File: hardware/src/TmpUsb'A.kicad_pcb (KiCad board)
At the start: 2 copper layers, 25 x 17 mm, 17 parts, among them P1 48037-2200, U1 PIC18F26J50

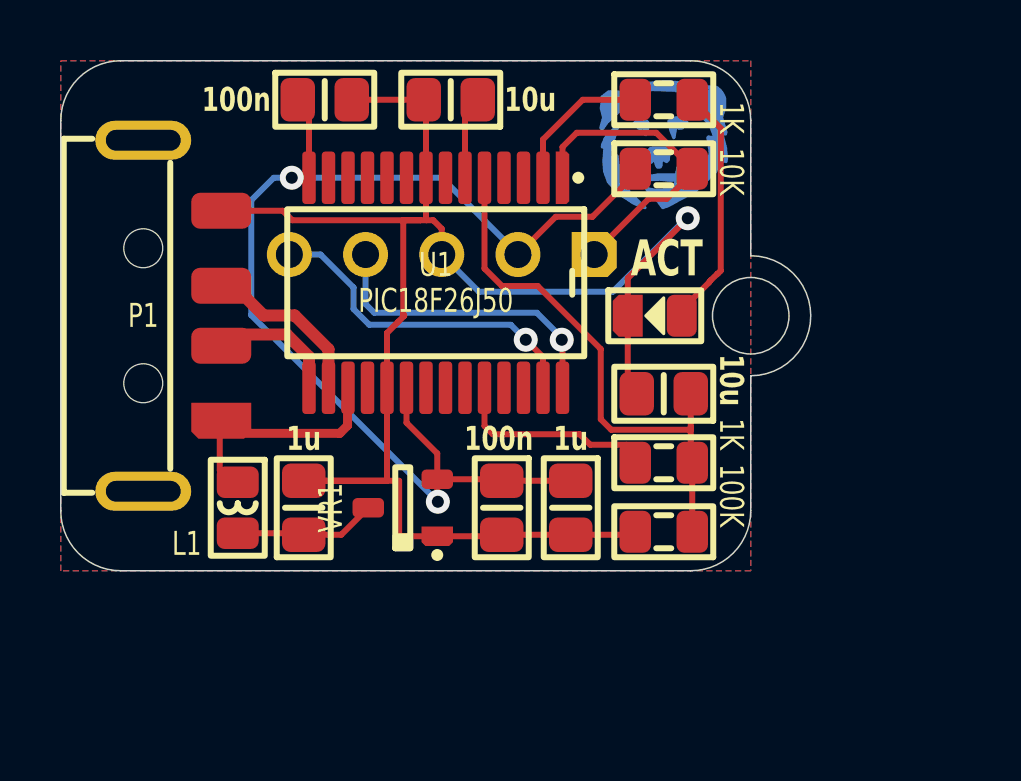
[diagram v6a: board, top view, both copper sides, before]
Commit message: Fixing connector designators
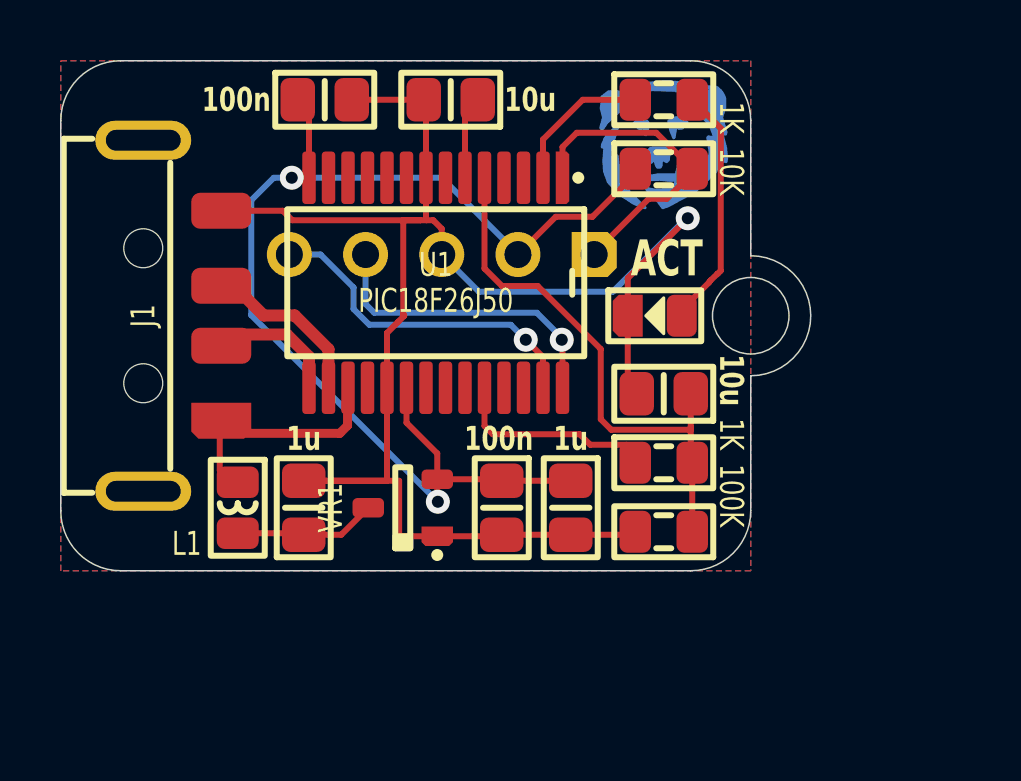
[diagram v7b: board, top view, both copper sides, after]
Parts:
- J1: renamed from P1; footprint Medo64:P USB A 2.0 (4w) -> Medo64:J USB A 2.0 Plug (4w)
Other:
- rule pad_to_mask_clearance: 0 -> 0.05
- board text added: "TmpUsb'A BXXXX"
- board text removed: "TmpUsb'A B"
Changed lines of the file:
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@@
 			(dielectric_constraints no)
 		)
-		(pad_to_mask_clearance 0)
+		(pad_to_mask_clearance 0.05)
 		(allow_soldermask_bridges_in_footprints no)
 		(aux_axis_origin 15 15)
@@
 		)
 	)
-	(footprint "Medo64:P USB A 2.0 (4w)"
+	(footprint "Medo64:J USB A 2.0 Plug (4w)"
 		(layer "F.Cu")
 		(at 17.75 23.5 -90)
-		(property "Reference" "P1"
-			(at 0 0 0)
-			(unlocked yes)
+		(property "Reference" "J1"
+			(at 0 0 -90)
 			(layer "F.SilkS")
 			(effects
@@
 		(property "Value" "48037-2200"
 			(at 0 1.6 -90)
-			(unlocked yes)
 			(layer "F.SilkS")
 			(hide yes)
@@
 			)
 		)
-		(property "Footprint" "Medo64:P USB A 2.0 (4w)"
+		(property "Footprint" "Medo64:J USB A 2.0 Plug (4w)"
 			(at 0 0 -90)
 			(unlocked yes)
@@
 			(layer "F.Fab")
 		)
-		(fp_text user "D-"
-			(at 1 -1.5 -90)
-			(unlocked yes)
+		(fp_text user "Vbus"
+			(at 3.5 -1.4 -90)
 			(layer "Cmts.User" knockout)
 			(effects
@@
 					(size 0.13 0.07)
 					(thickness 0.01)
+					(bold yes)
 				)
-				(justify top)
 			)
 		)
 		(fp_text user "GND"
-			(at -3.5 -1.5 -90)
-			(unlocked yes)
+			(at -3.5 -1.4 -90)
 			(layer "Cmts.User" knockout)
 			(effects
@@
 					(bold yes)
 				)
-				(justify top)
 			)
 		)
-		(fp_text user "Vbus"
-			(at 3.5 -1.5 -90)
-			(unlocked yes)
+		(fp_text user "D-"
+			(at 1 -1.4 -90)
 			(layer "Cmts.User" knockout)
 			(effects
@@
 					(size 0.13 0.07)
 					(thickness 0.01)
-					(bold yes)
 				)
-				(justify top)
 			)
 		)
 		(fp_text user "D+"
-			(at -1 -1.5 -90)
-			(unlocked yes)
+			(at -1 -1.4 -90)
 			(layer "Cmts.User" knockout)
 			(effects
@@
 					(thickness 0.01)
 				)
-				(justify top)
 			)
 		)
@@
 		(layer "Edge.Cuts")
 	)
-	(gr_text "TmpUsb'A B"
+	(gr_text "TmpUsb'A BXXXX"
 		(at 37.2 31.4 0)
 		(layer "B.SilkS")
